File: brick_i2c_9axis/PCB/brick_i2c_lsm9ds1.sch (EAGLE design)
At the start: 9 parts, among them J1 BRICK_I2C

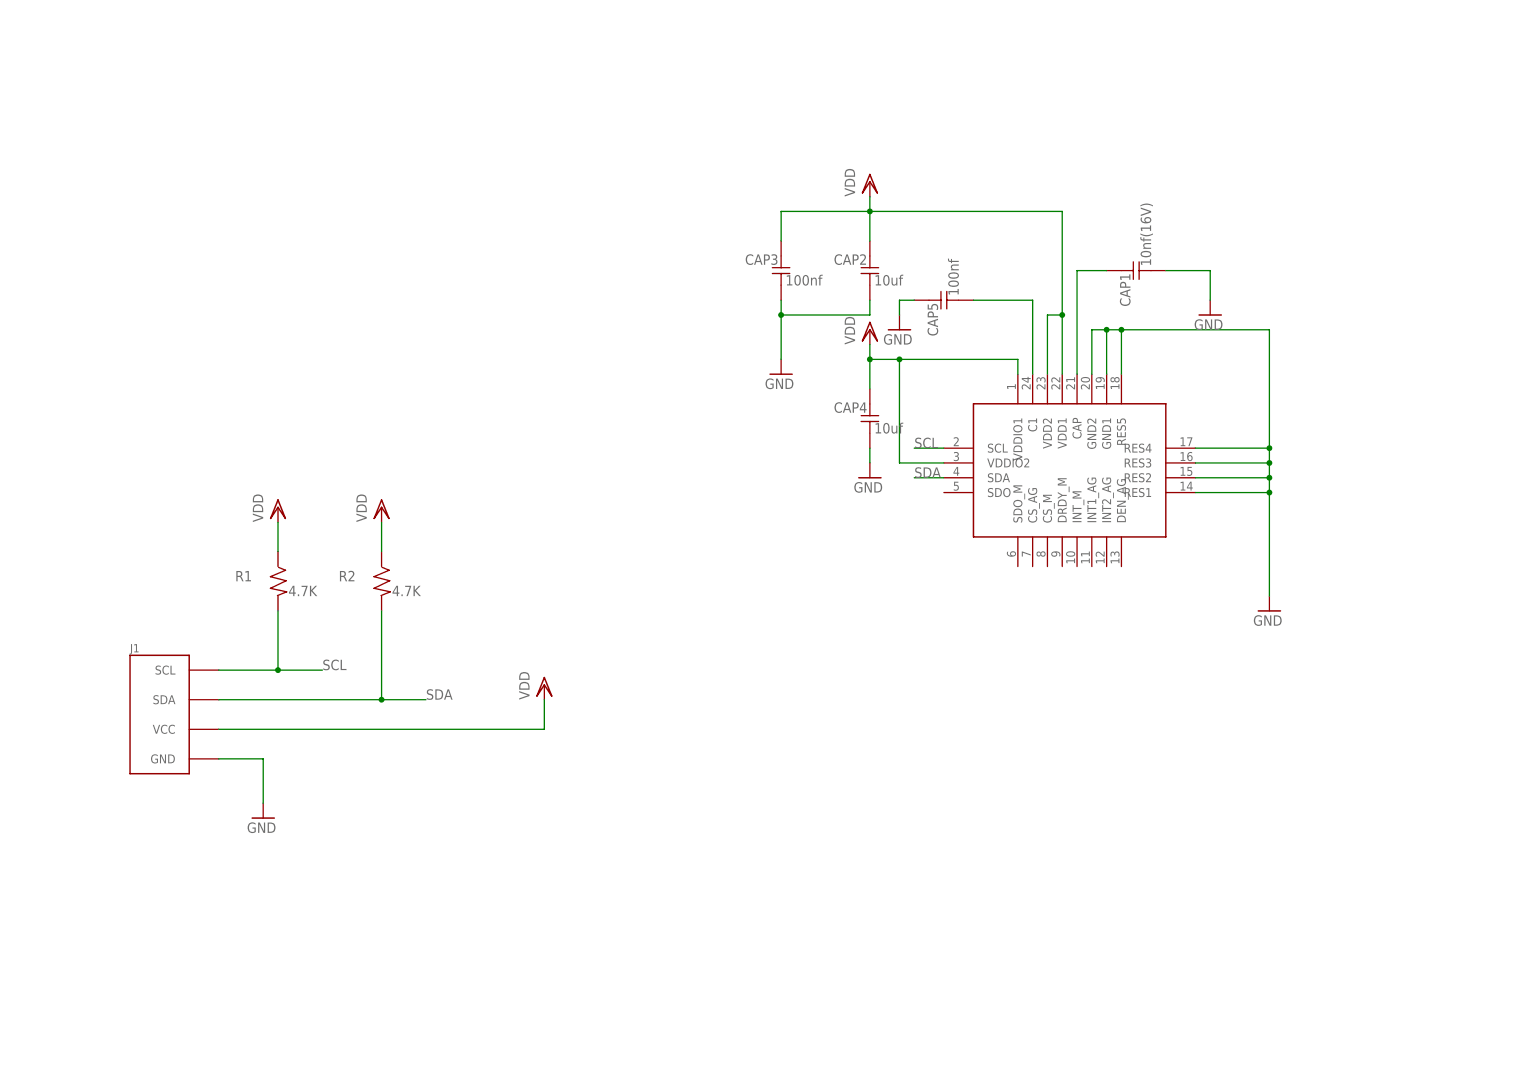
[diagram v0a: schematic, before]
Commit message: Modified for Elecrow
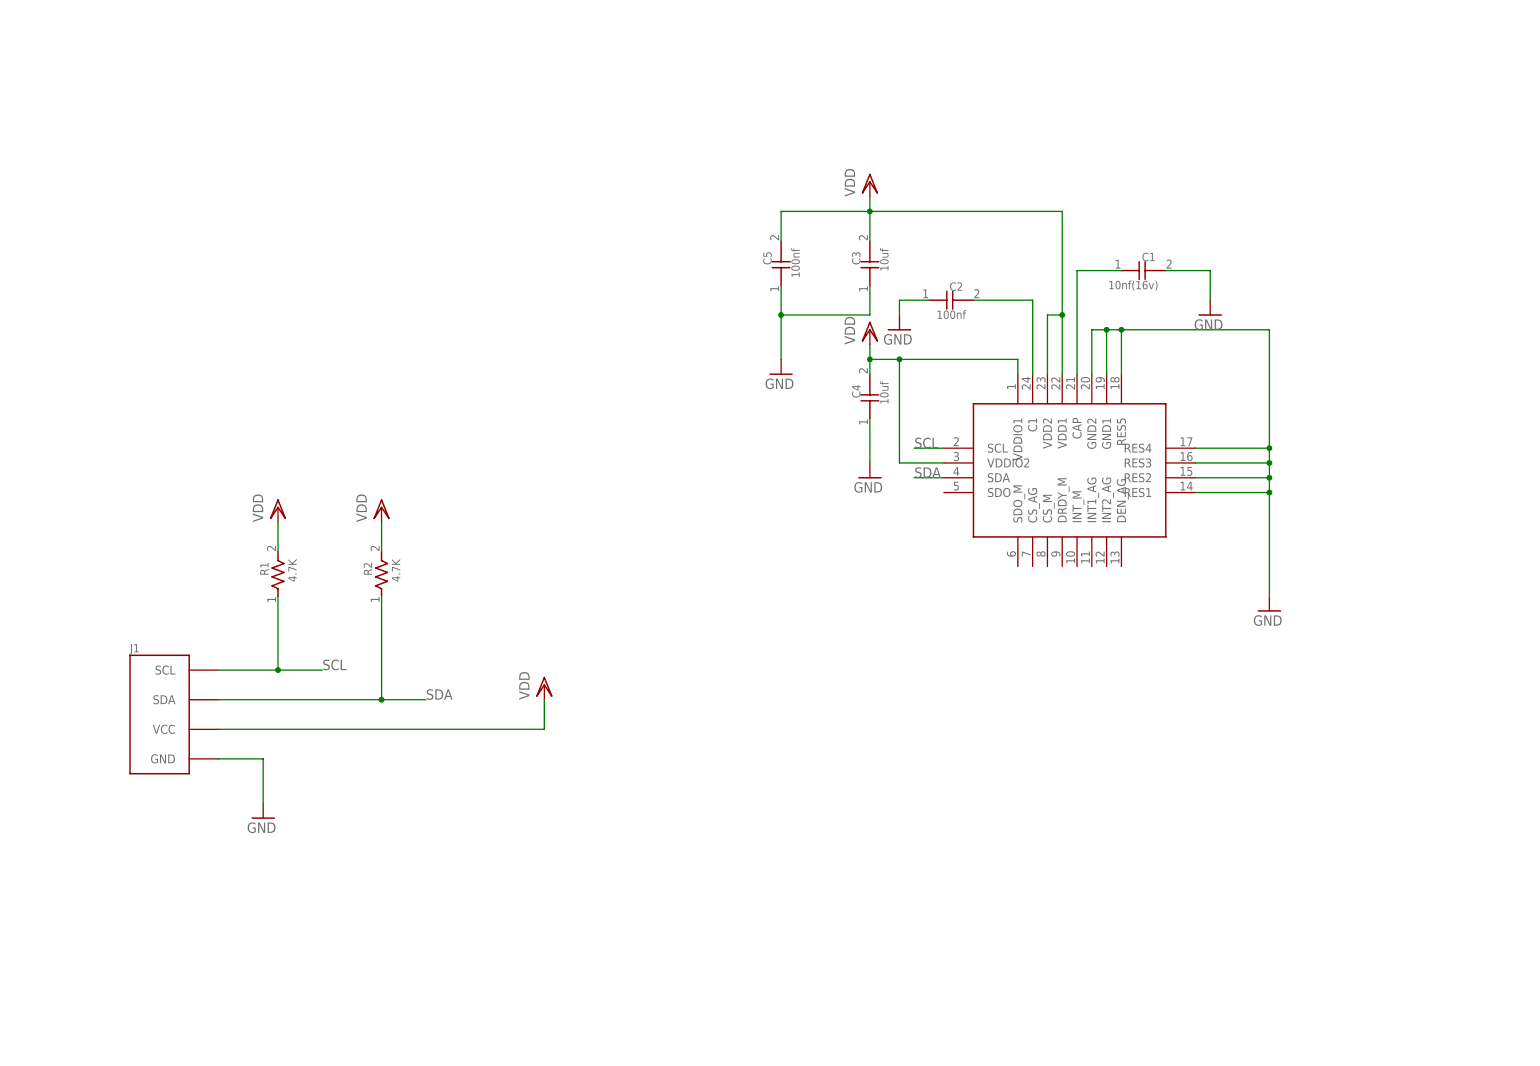
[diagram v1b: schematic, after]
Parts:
- removed CAP1: 10nf(16V), gclueParts:CAPACITOR-0603
- removed CAP2, CAP4: 10uf, gclueParts:CAPACITOR-0603
- removed CAP3, CAP5: 100nf, gclueParts:CAPACITOR-0603
- removed U$3: ST-LSM9DS1TR, gclueSensor:ST-LSM9DS1TR
- added C1: 10nf(16v), GClue-Capacitor:CAPACITOR0603
- added C2, C5: 100nf, GClue-Capacitor:CAPACITOR0603
- added C3, C4: 10uf, GClue-Capacitor:CAPACITOR0603
- added U$1: ST-LSM9DS1TR, GClue-Mems:ST-LSM9DS1TR
- R1, R2: device gclueParts:RESISTOR-0603 -> GClue-Resistors:RESISTOR0603
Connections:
- net GND: now also C1.2, C2.1, C3.1, C4.1, C5.1, U$1.GND1, U$1.GND2, U$1.RES1, U$1.RES2, U$1.RES3, U$1.RES4, U$1.RES5; no longer CAP1.P$1, CAP2.P$1, CAP3.P$1, CAP4.P$1, CAP5.P$2, U$3.GND1, U$3.GND2, U$3.RES1, U$3.RES2, U$3.RES3, U$3.RES4, U$3.RES5
- net N$1: now also C1.1, U$1.CAP; no longer CAP1.P$2, U$3.CAP
- net N$6: now also C2.2, U$1.C1; no longer CAP5.P$1, U$3.C1
- net SCL: now also R1.1, U$1.SCL; no longer R1.P$1, U$3.SCL
- net SDA: now also R2.1, U$1.SDA; no longer R2.P$1, U$3.SDA
- net VDD: now also C3.2, C4.2, C5.2, R1.2, R2.2, U$1.VDD1, U$1.VDD2, U$1.VDDIO1, U$1.VDDIO2; no longer CAP2.P$2, CAP3.P$2, CAP4.P$2, R1.P$2, R2.P$2, U$3.VDD1, U$3.VDD2, U$3.VDDIO1, U$3.VDDIO2

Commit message: Update for elecrow
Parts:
- added U$3: (no value), gclue:LOGO_GCLUE-M
- added U$4: (no value), gclue:LOGO_OSHW-M
- J1: value BRICK_I2C -> (none)
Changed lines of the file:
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@@
 </classes>
 <parts>
-<part name="J1" library="gclue" deviceset="BRICK_I2C" device=""/>
 <part name="U$2" library="gclue" deviceset="A4L-LOC" device=""/>
 <part name="GND9" library="gclue" deviceset="GND" device=""/>
@@
 <part name="C4" library="GClue-Capacitor" deviceset="CAPACITOR" device="0603" value="10uf"/>
 <part name="C5" library="GClue-Capacitor" deviceset="CAPACITOR" device="0603" value="100nf"/>
+<part name="J1" library="gclue" deviceset="BRICK_I2C" device=""/>
+<part name="U$3" library="gclue" deviceset="LOGO_GCLUE" device="-M"/>
+<part name="U$4" library="gclue" deviceset="LOGO_OSHW" device="-M"/>
 </parts>
 <sheets>
@@
 </plain>
 <instances>
-<instance part="J1" gate="G$1" x="30.48" y="58.42"/>
 <instance part="U$2" gate="G$1" x="2.54" y="0"/>
 <instance part="GND9" gate="GND" x="218.44" y="78.74"/>
@@
 <instance part="C4" gate="G$1" x="149.86" y="111.76" rot="R90"/>
 <instance part="C5" gate="G$1" x="134.62" y="134.62" rot="R90"/>
+<instance part="J1" gate="G$1" x="30.48" y="58.42"/>
+<instance part="U$3" gate="G$1" x="180.34" y="10.16"/>
+<instance part="U$4" gate="G$1" x="200.66" y="12.7"/>
 </instances>
 <busses>
@@
 </segment>
 <segment>
-<pinref part="J1" gate="G$1" pin="GND"/>
 <wire x1="38.1" y1="50.8" x2="45.72" y2="50.8" width="0.1524" layer="91"/>
 <wire x1="45.72" y1="50.8" x2="45.72" y2="43.18" width="0.1524" layer="91"/>
 <pinref part="GND4" gate="GND" pin="GND"/>
+<pinref part="J1" gate="G$1" pin="GND"/>
 </segment>
 </net>
 <net name="SDA" class="0">
 <segment>
-<pinref part="J1" gate="G$1" pin="SDA"/>
 <wire x1="38.1" y1="60.96" x2="66.04" y2="60.96" width="0.1524" layer="91"/>
 <label x="73.66" y="60.96" size="1.778" layer="95"/>
@@
 <junction x="66.04" y="60.96"/>
 <pinref part="R2" gate="G$1" pin="1"/>
+<pinref part="J1" gate="G$1" pin="SDA"/>
 </segment>
 <segment>
@@
 <net name="SCL" class="0">
 <segment>
-<pinref part="J1" gate="G$1" pin="SCL"/>
 <wire x1="38.1" y1="66.04" x2="48.26" y2="66.04" width="0.1524" layer="91"/>
 <label x="55.88" y="66.04" size="1.778" layer="95"/>
@@
 <junction x="48.26" y="66.04"/>
 <pinref part="R1" gate="G$1" pin="1"/>
+<pinref part="J1" gate="G$1" pin="SCL"/>
 </segment>
 <segment>
@@
 </segment>
 <segment>
-<pinref part="J1" gate="G$1" pin="VCC"/>
 <wire x1="38.1" y1="55.88" x2="93.98" y2="55.88" width="0.1524" layer="91"/>
 <wire x1="93.98" y1="55.88" x2="93.98" y2="60.96" width="0.1524" layer="91"/>
 <pinref part="VDD3" gate="G$1" pin="VDD"/>
-</segment>
-<segment>
+<pinref part="J1" gate="G$1" pin="VCC"/>
+</segment>
+<segment>

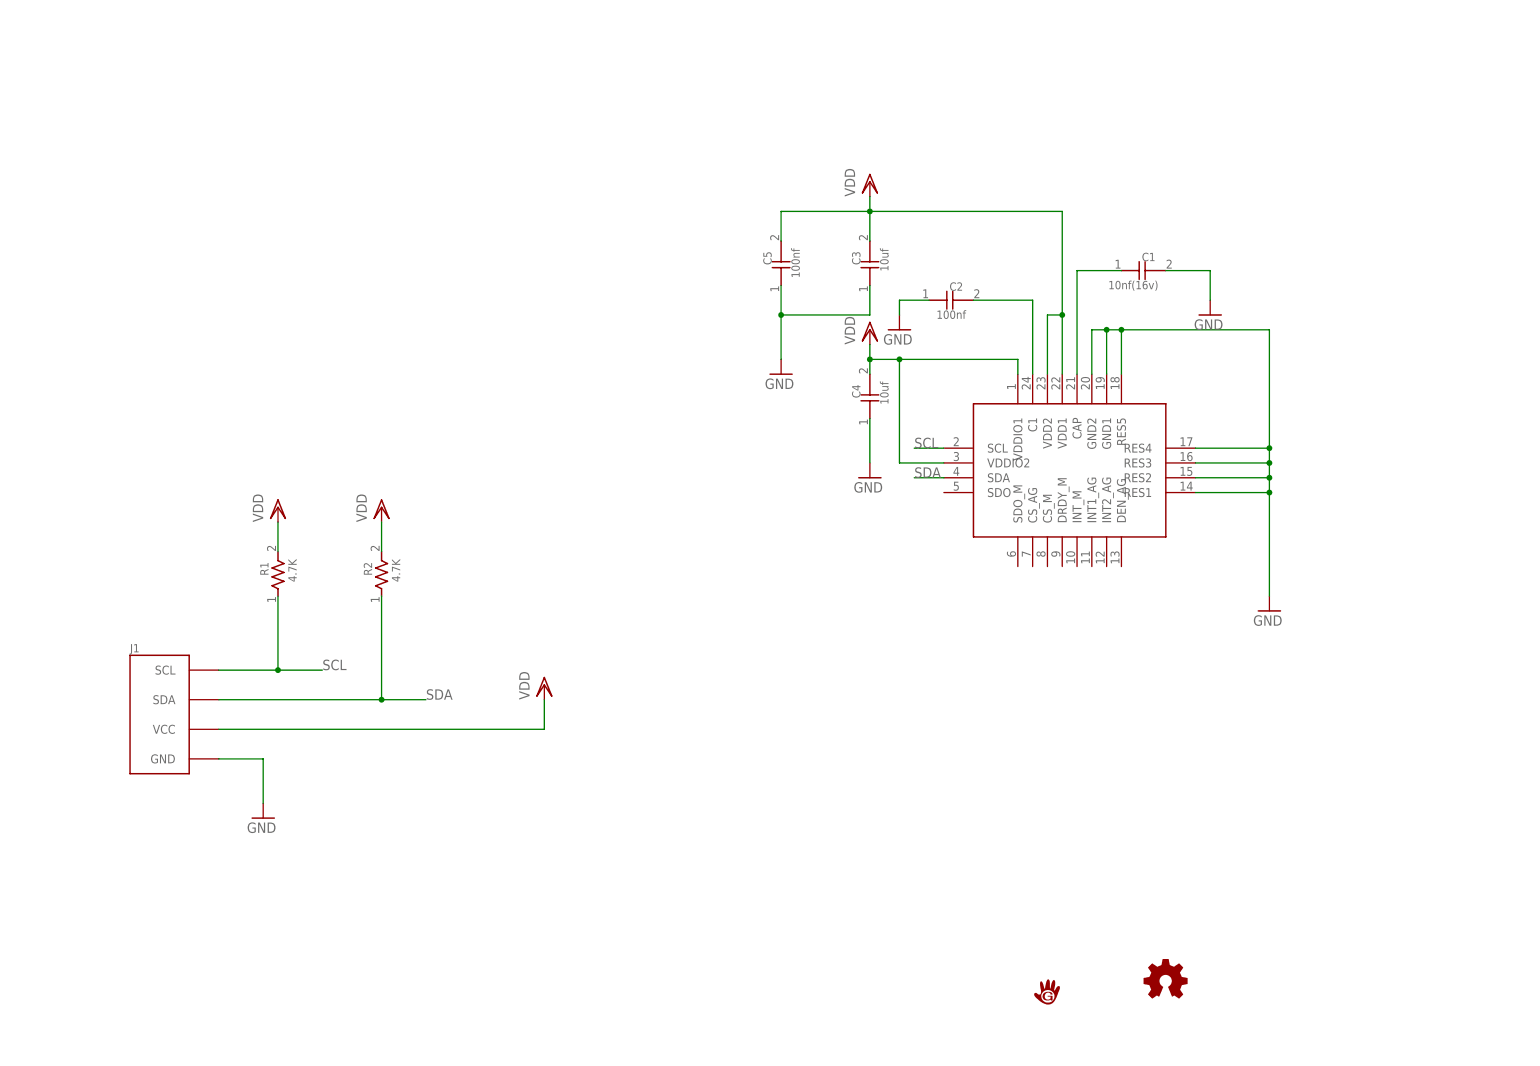
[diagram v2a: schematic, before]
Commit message: refine board size brick_i2c_9axis
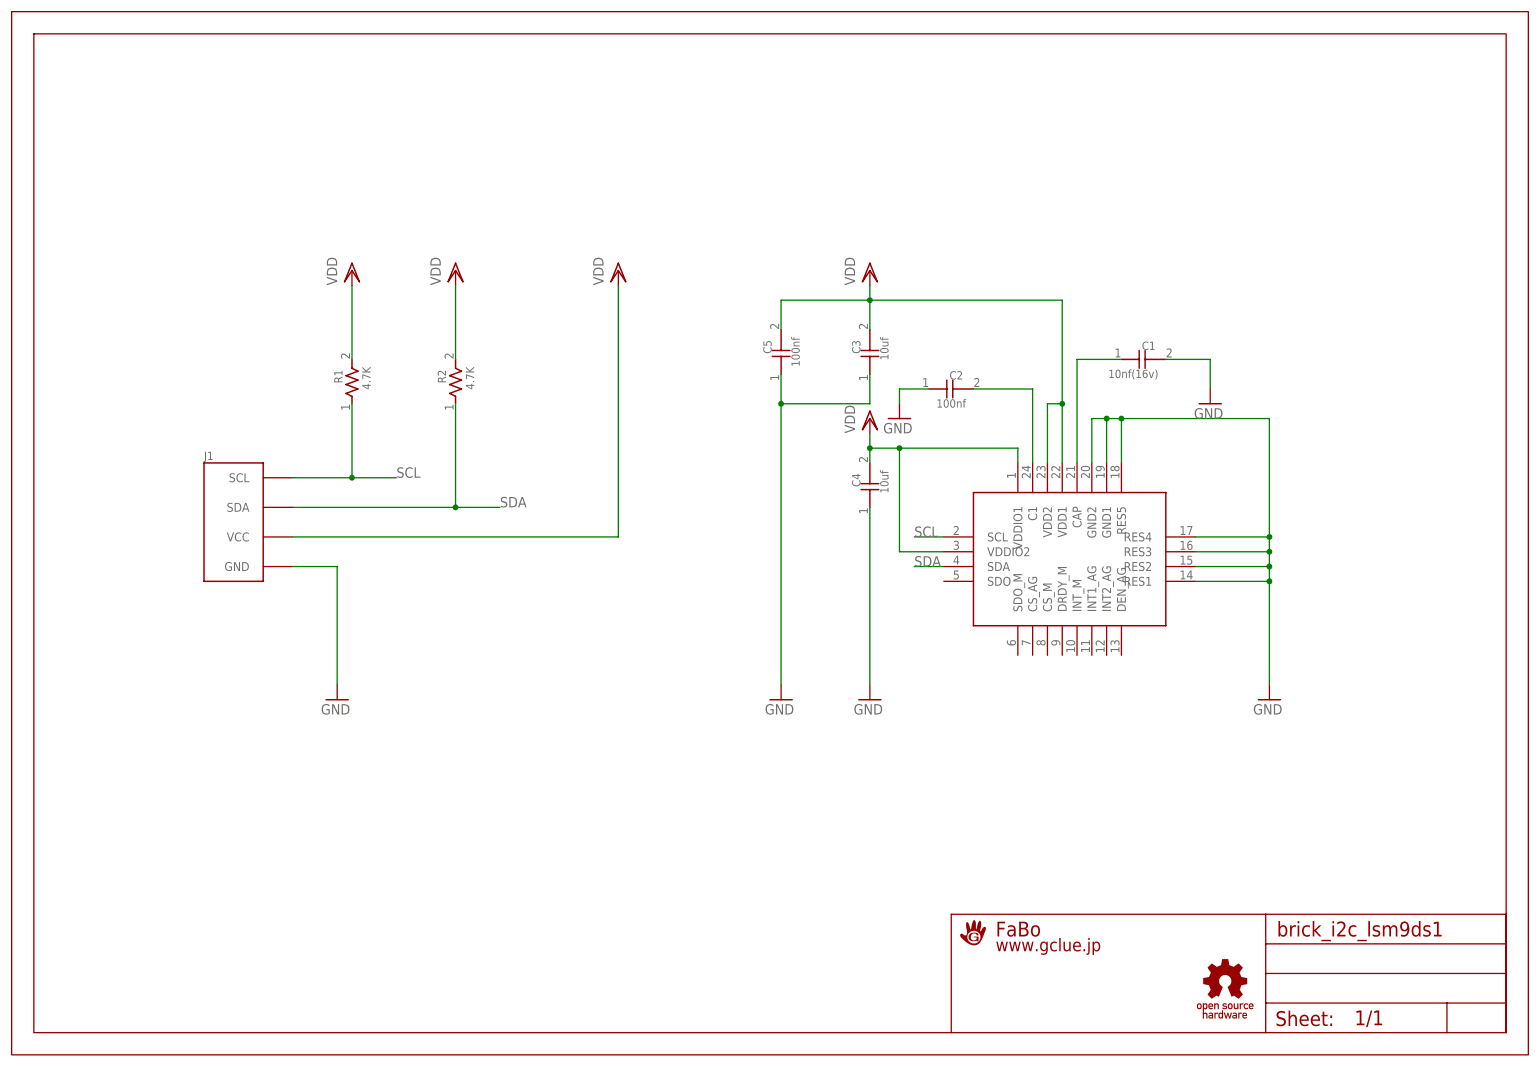
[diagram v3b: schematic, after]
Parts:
- removed U$4: (no value), gclue:LOGO_OSHW-M
- added U$2: A4L-LOC-FABO_M, gclue:A4L-LOC-FABO_M
- U$3: device gclue:LOGO_GCLUE-M -> gclue:LOGO_OSHW_T-M
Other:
- moved on the sheet: C1, C2, C3, C4, C5, J1, R1, R2

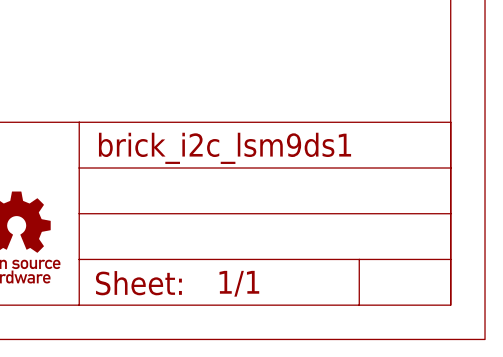
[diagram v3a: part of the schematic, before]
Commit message: change revision number beta->beta2
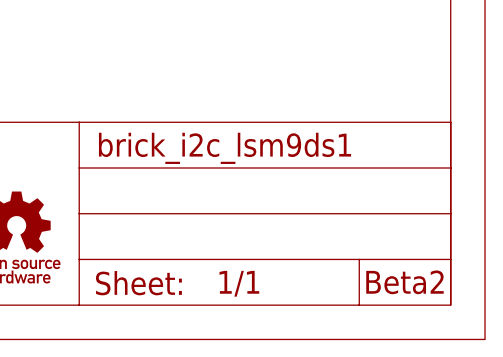
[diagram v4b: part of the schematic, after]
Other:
- note added: "Beta2"
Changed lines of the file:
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@@
 <sheet>
 <plain>
+<text x="254" y="5.08" size="2.54" layer="94" align="bottom-center">Beta2</text>
 </plain>
 <instances>
